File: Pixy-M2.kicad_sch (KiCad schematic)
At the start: 28 parts, among them J1 USB_C_Receptacle_USB2.0_14P, J2 Conn_01x22_Pin, J3 Conn_01x22_Pin, SW1 SW_Push, SW2 SW_Push, U1 ESP32-S3-WROOM-1-N16, U2 USBLC6-2SC6, U3 AP63203WU

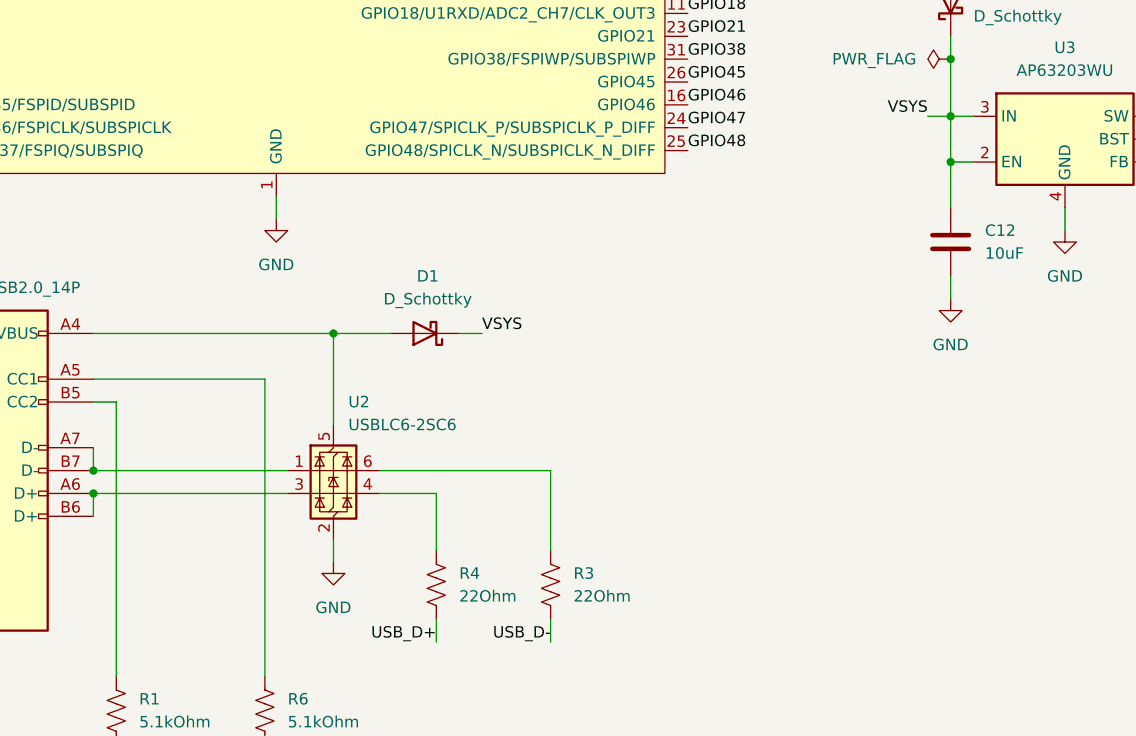
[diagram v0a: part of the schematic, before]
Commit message: Add undervoltage lockout for the 2S LiPo (open issue 2)
U3.2 (EN) and U3.3 (IN) were the same net, so the AP63203WU could never turn
itself off. The ESP32 would keep drawing from the pack until the cells were
damaged, with the usual LiPo failure modes on the next recharge. EN is now
driven by a programmed UVLO network, and VSYS carries U3.3 (IN) only.

    VBAT ---[R7 120k]---+--------------- U3.2 (EN)      net: REG_EN
                        |
    VBUS ---|<|---[R9 39k]                              D3 = BAT54W
             D3         |
                        +---[R8 24k]--- GND
                        +---[C13 100nF]--- GND

New parts: R7 120kOhm 1%, R8 24kOhm 1%, R9 39kOhm 1% (0805),
           C13 0.1uF 50V (0603), D3 BAT54W (SOD-123).

Why not the divider the notes prescribed
----------------------------------------
CLAUDE.md called for 220k/47k from VSYS to EN, giving ~6.25V turn-on. That
would have bricked USB-only operation. USB supplies VSYS through D1, so
VSYS = 5.0 - 0.35 = 4.65V, putting EN at 4.65 * 47/267 = 0.82V - below the
1.15V minimum threshold. The board could never have been programmed or
bench-tested without a charged pack installed, which is a bad trait for a
board whose USB port exists to program it.

Sensing VBAT ahead of D2 instead also removes D2's load-dependent forward
drop from the measurement, which would otherwise smear the threshold by
roughly +/-0.075 V/cell depending on how much current the board was drawing.

Why this is not a crude divider
-------------------------------
The AP63203 has a purpose-built UVLO input (datasheet DS41326 Rev 3-2,
Fig. 22, Eq. 1/2). A 1.5uA source pulls up on EN at all times and a further
4uA switches in once the part is enabled, so the hysteresis is designed
rather than incidental. Thresholds are VEN_H 1.15/1.18/1.23V rising and
VEN_L 1.05/1.10/1.15V falling. R7/R8 were solved from those equations:

    turn-on    1.18V at VBAT = 6.90V   (3.45 V/cell)
    turn-off   1.10V at VBAT = 5.94V   (2.97 V/cell)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
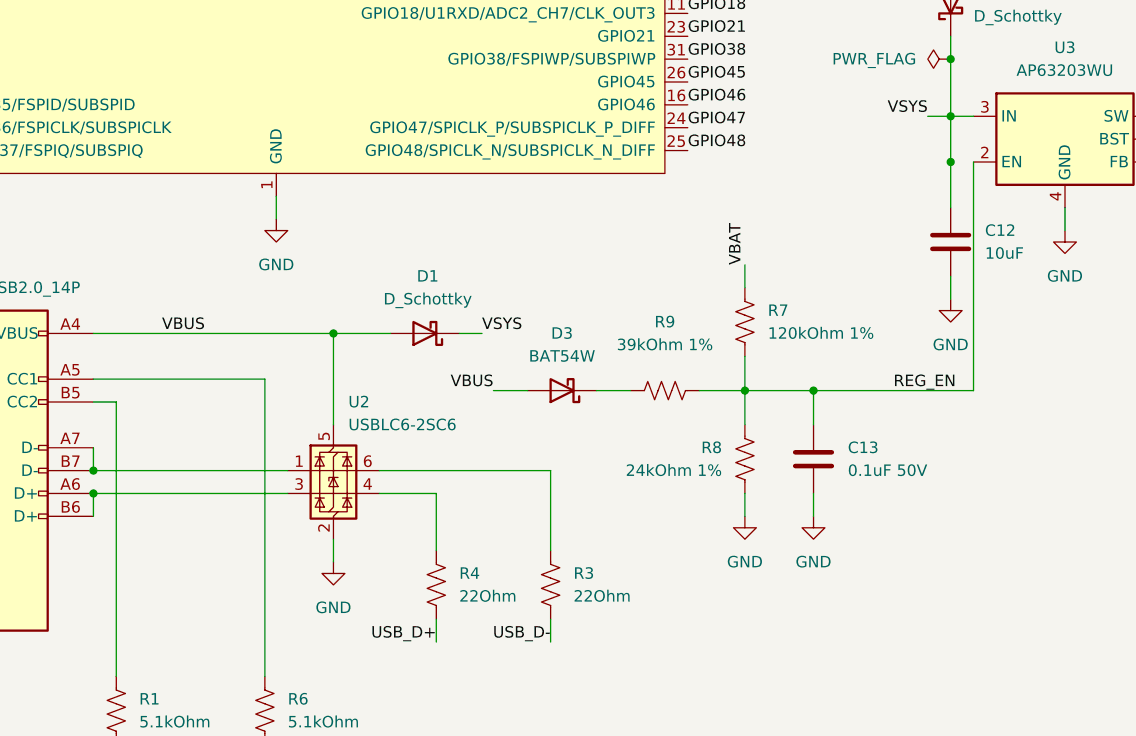
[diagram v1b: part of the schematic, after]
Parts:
- added C13: 0.1uF 50V, Capacitor_SMD:C_0603_1608Metric, symbol Device:C
- added D3: BAT54W, Diode_SMD:D_SOD-123, symbol Device:D_Schottky
- added R7: 120kOhm 1%, Resistor_SMD:R_0805_2012Metric, symbol Device:R_US
- added R8: 24kOhm 1%, Resistor_SMD:R_0805_2012Metric, symbol Device:R_US
- added R9: 39kOhm 1%, Resistor_SMD:R_0805_2012Metric, symbol Device:R_US
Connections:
- net GND: now also C13.2, R8.2
- net VBAT: now also R7.1
- net VSYS: no longer U3.2 (EN)
- net VBUS: now reaches D1.2 (A), J1.A4 (VBUS), J1.A9 (VBUS), J1.B4 (VBUS), J1.B9 (VBUS), U2.5 (VBUS)
- net VBUS: now also D3.2 (A)
- new net: D3.1 (K), R9.1
- new net REG_EN: C13.1, R7.2, R8.1, R9.2, U3.2 (EN)

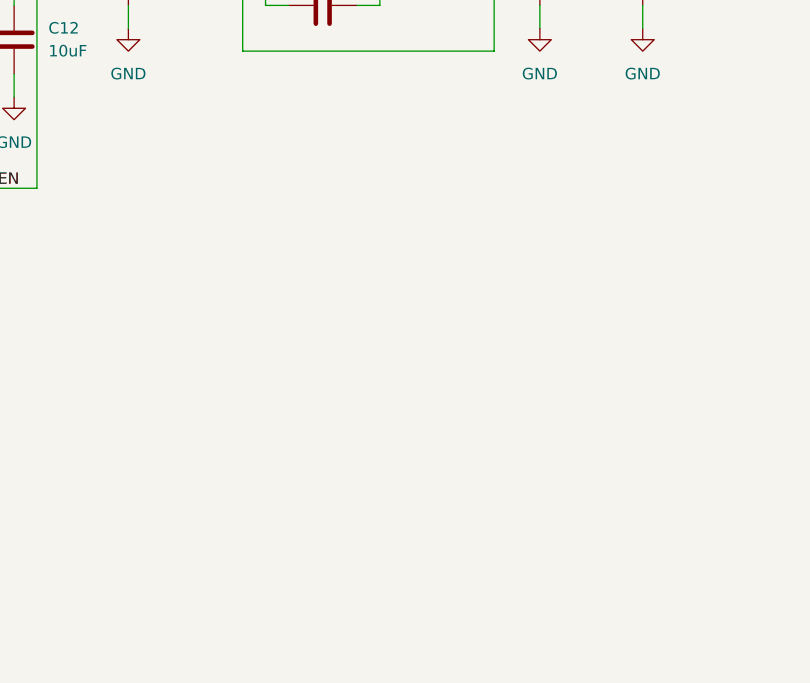
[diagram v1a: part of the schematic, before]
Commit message: Add battery sense divider into ADC1 (open issue 5)
VBAT_SENSE was a label on U1.39 and nothing else - a single-pin net - so the
MCU had no way to read pack voltage. It can now:

    VBAT --[R10 470k]--+--> U1.39   GPIO1 / ADC1_CH0
                       |
                  [R11 220k]   [C14 100nF]
                       |            |
                      GND          GND

New parts: R10 470kOhm 1%, R11 220kOhm 1% (0805), C14 0.1uF 50V (0603).

This matters because issue 2's hardware UVLO is deliberately defeated whenever
USB is connected, and its battery-only cutoff carries a +/-0.15 V/cell
tolerance spread. Firmware is the accurate mechanism and until now it was
blind. GPIO1 is ADC1_CH0; ADC2 is unusable while Wi-Fi is active, so this must
not be moved to an ADC2 pin. Firmware should use ADC_ATTEN_DB_12.

    pack 8.4V full      4.20 V/cell   ->  2.678 V at the ADC
    pack 7.4V nominal   3.70 V/cell   ->  2.359 V
    pack 6.90V (UVLO on)3.45 V/cell   ->  2.200 V
    pack 5.94V (cutoff) 2.97 V/cell   ->  1.894 V
    pack 9.5V overcharge4.75 V/cell   ->  3.029 V

422 mV of headroom at a full pack. An overcharged pack still lands inside the
attenuator's 3100 mV range rather than railing, so an over-voltage fault stays
measurable instead of just clipping.

Why not the 100k/47k + MOSFET gate the notes specified
------------------------------------------------------
Two reasons, one of them a safety problem.

First, the gate as described would damage the ADC pin. A low-side MOSFET - the
obvious reading of "gate the divider with a small MOSFET" - switches the bottom
of the divider but leaves the top tied to VBAT. With the FET off the sense node
floats up until GPIO1's ESD clamp conducts at ~3.6V, injecting ~46uA into the
3.3V rail through the pin, and still draining the pack. It defeats its own
purpose while stressing the input. Gating a divider whose top sits above the
ADC's limit has to be done on the high side, which needs a P-FET plus an N-FET
level shifter, becaus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
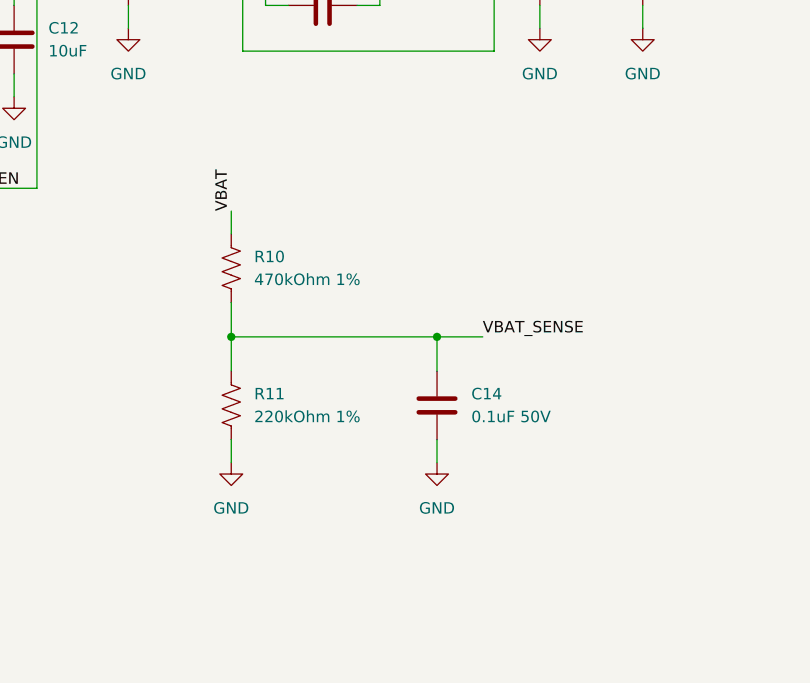
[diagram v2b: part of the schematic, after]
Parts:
- added C14: 0.1uF 50V, Capacitor_SMD:C_0603_1608Metric, symbol Device:C
- added R10: 470kOhm 1%, Resistor_SMD:R_0805_2012Metric, symbol Device:R_US
- added R11: 220kOhm 1%, Resistor_SMD:R_0805_2012Metric, symbol Device:R_US
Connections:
- net GND: now also C14.2, R11.2
- net VBAT: now also R10.1
- net VBAT_SENSE: now also C14.1, R10.2, R11.1

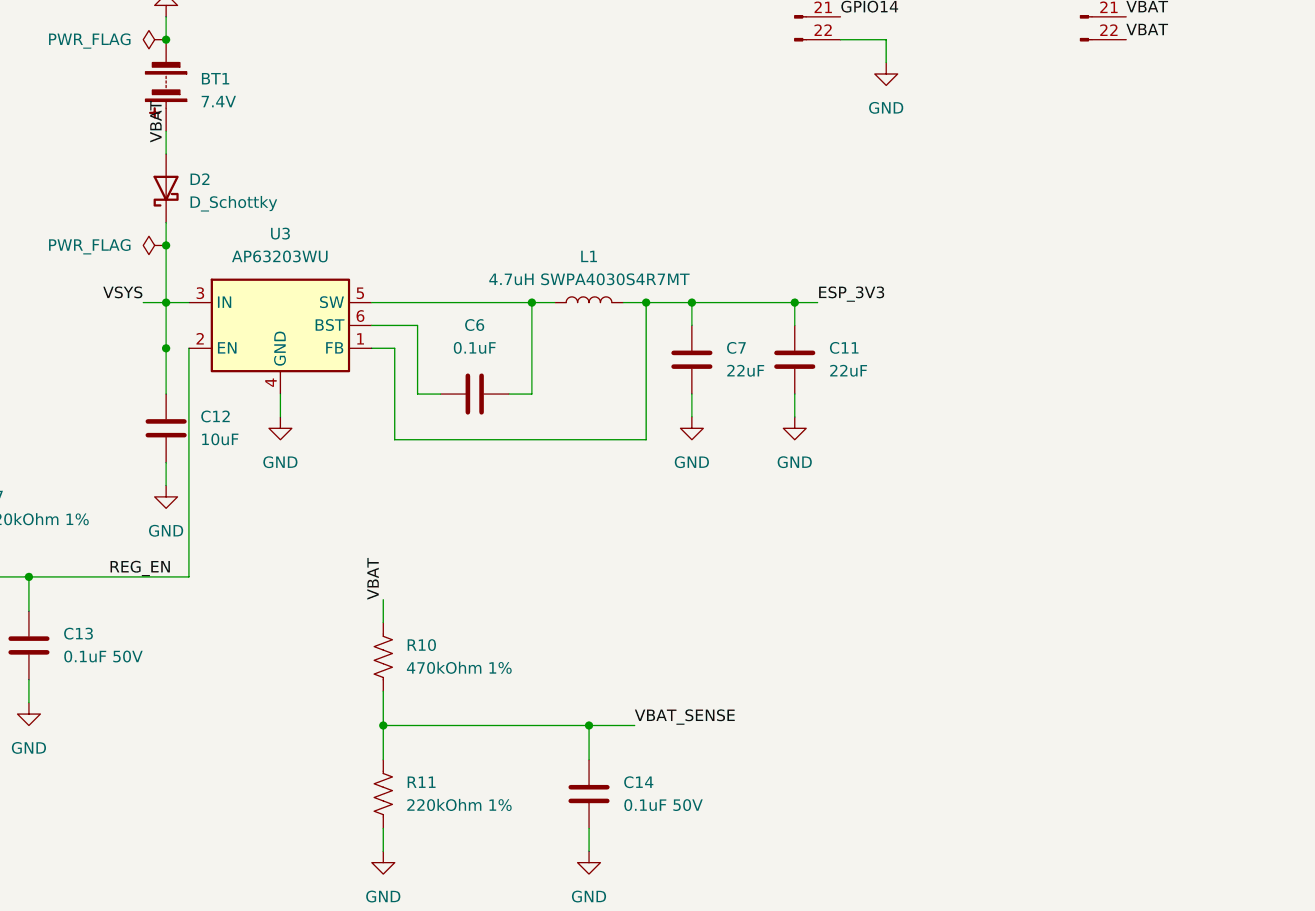
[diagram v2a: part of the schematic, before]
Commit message: Add indicator LEDs and test points (open issue 13)
Power LED:  ESP_3V3 -[R12 10k]- D4 (red)   -> GND, ~150uA
Status LED: GPIO3   -[R13 2.2k]- D5 (green) -> GND, ~550uA when lit
Test points: TP1 VBAT, TP2 3V3, TP3 GND, TP4 SW node

D4 is red because the specified 10k constrains the colour: at 3.3V a
10k resistor delivers (3.3 - Vf)/10k, so a pure-green InGaN part
(Vf ~3.1V) would draw ~10uA and not light. Red (Vf ~1.7-1.9V) gives
~150uA. Blue/white/pure-green cannot be substituted without changing
the resistor.

D5 sits on GPIO3, the only one of the three floating strapping pins
that issue 12 found safe to repurpose, and is wired active-high so
the pin stays at 0V at reset via its internal pulldown -- GPIO3's
safe strapping state. This clears its isolated_pin_label warning;
ERC is now 0 errors / 2 warnings (GPIO45, GPIO46).

R13 is 2.2k rather than 10k: it is firmware-gated so it costs nothing
when off, and 10k would have been marginal for visibility.

TP4 is wired onto the U3.5-L1.1 run directly rather than via a label,
so Net-(U3-SW) keeps its auto-generated name. It is in tension with
the "keep the SW copper island small" layout rule; noted in CLAUDE.md
as the part to drop if the island ends up marginal.

Verified: netlist diff shows only the intended changes, ERC 0 errors /
2 warnings, all 44 components have footprints, re-export is stable,
and the sheet was rendered and inspected.

Co-Authored-By: Claude Opus 5 <noreply@anthropic.com>
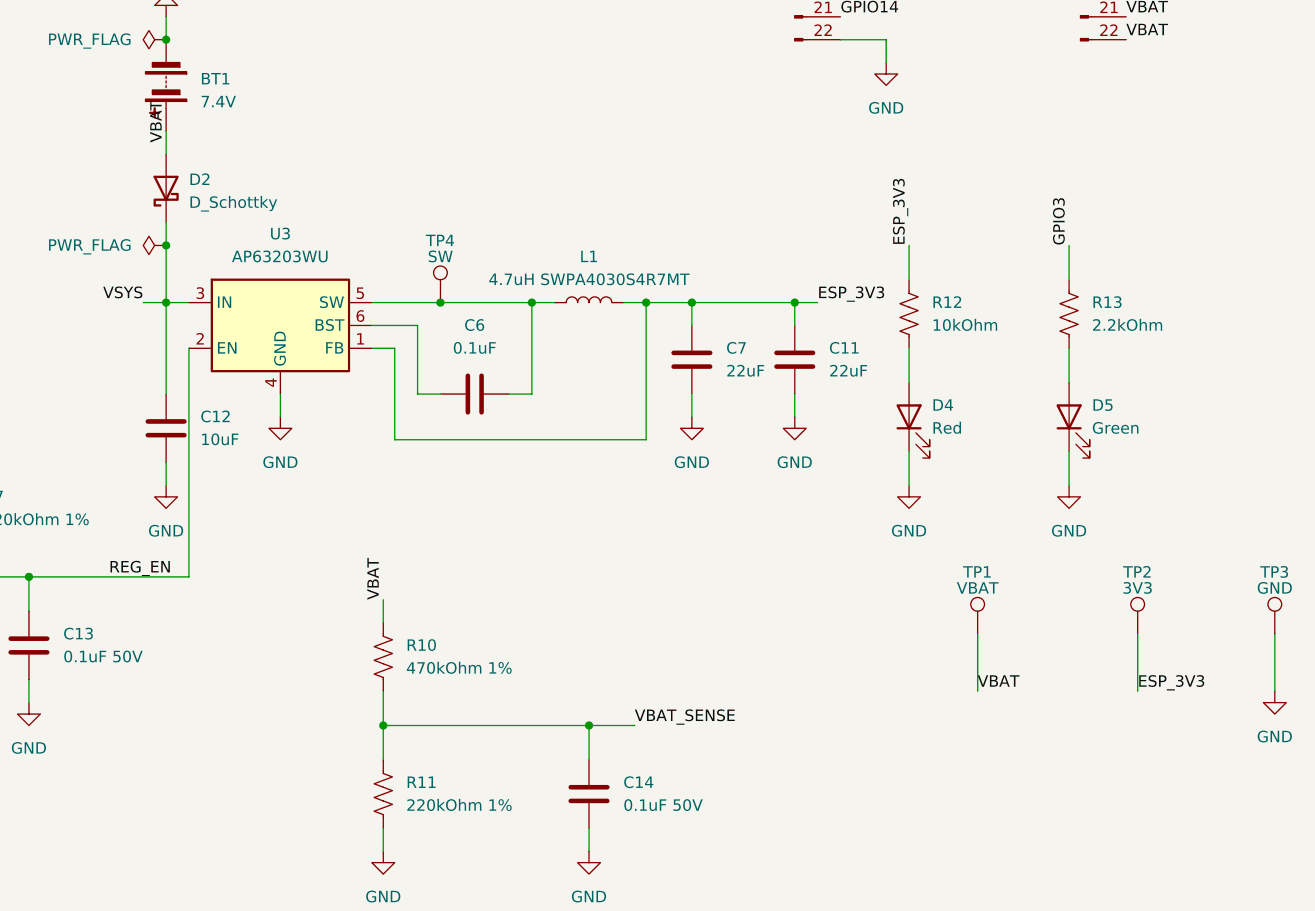
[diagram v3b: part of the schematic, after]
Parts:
- added D4: Red, LED_SMD:LED_0805_2012Metric, symbol Device:LED
- added D5: Green, LED_SMD:LED_0805_2012Metric, symbol Device:LED
- added R12: 10kOhm, Resistor_SMD:R_0805_2012Metric, symbol Device:R_US
- added R13: 2.2kOhm, Resistor_SMD:R_0805_2012Metric, symbol Device:R_US
- added TP1: VBAT, TestPoint:TestPoint_Pad_D1.5mm, symbol Connector:TestPoint
- added TP2: 3V3, TestPoint:TestPoint_Pad_D1.5mm, symbol Connector:TestPoint
- added TP3: GND, TestPoint:TestPoint_Pad_D1.5mm, symbol Connector:TestPoint
- added TP4: SW, TestPoint:TestPoint_Pad_D1.5mm, symbol Connector:TestPoint
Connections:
- net ESP_3V3: now also R12.1, TP2.1
- net GND: now also D4.1 (K), D5.1 (K), TP3.1
- net GPIO3: now also R13.1
- net VBAT: now also TP1.1
- net at C6.2, L1.1, U3.5 (SW): now also TP4.1
- new net: D4.2 (A), R12.2
- new net: D5.2 (A), R13.2
